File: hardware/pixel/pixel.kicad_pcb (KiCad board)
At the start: 2 copper layers, 20 x 20 mm, 13 parts, among them J1 IN (male), J2 OUT (female), U1 WS2814F

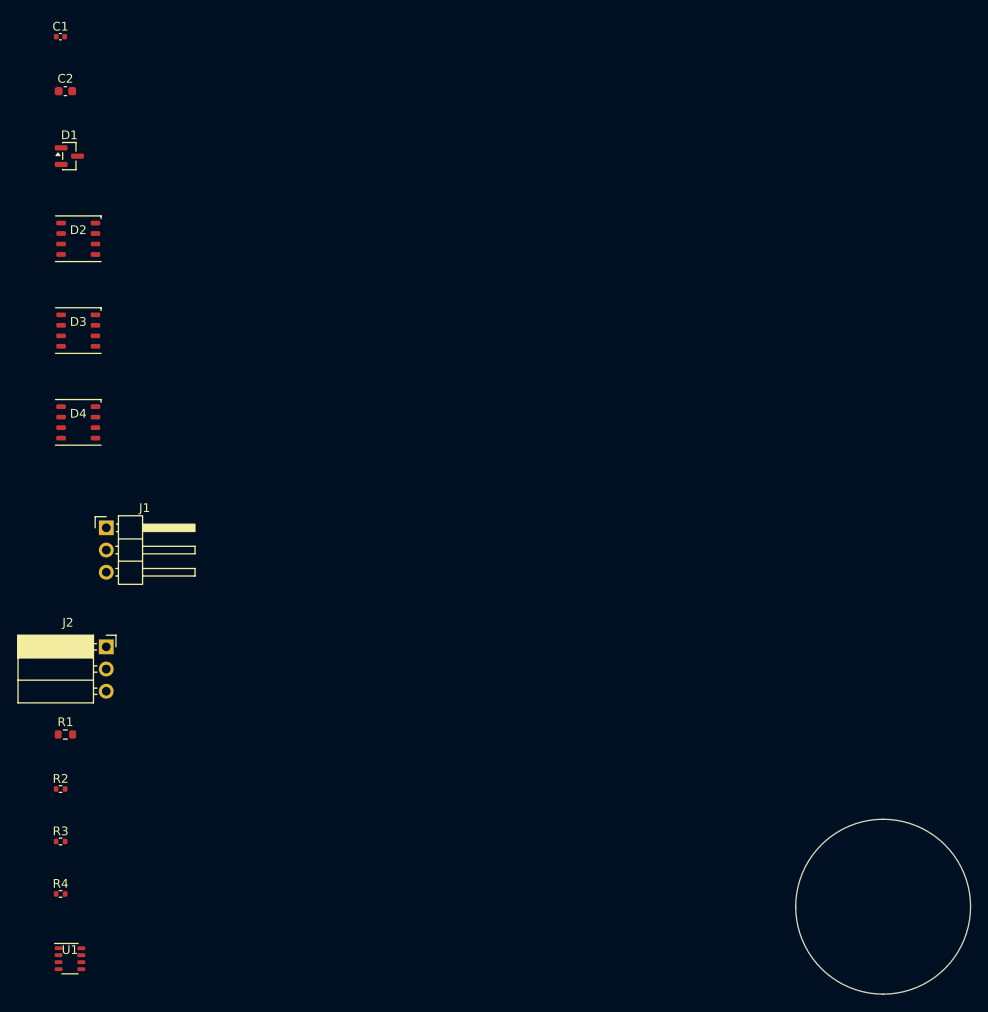
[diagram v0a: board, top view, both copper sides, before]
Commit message: Pixel PCB: provisional fit-study placement
Headers on the bottom along the south rim (estimated plug width),
LEDs in a centered triangle, U1 and passives around them. No
courtyard overlaps; only unrouted-connection DRC errors remain.
Also refreshes all footprints from their libraries (the schematic
import had left them out of sync).

Co-Authored-By: Claude Opus 5.5 <noreply@anthropic.com>
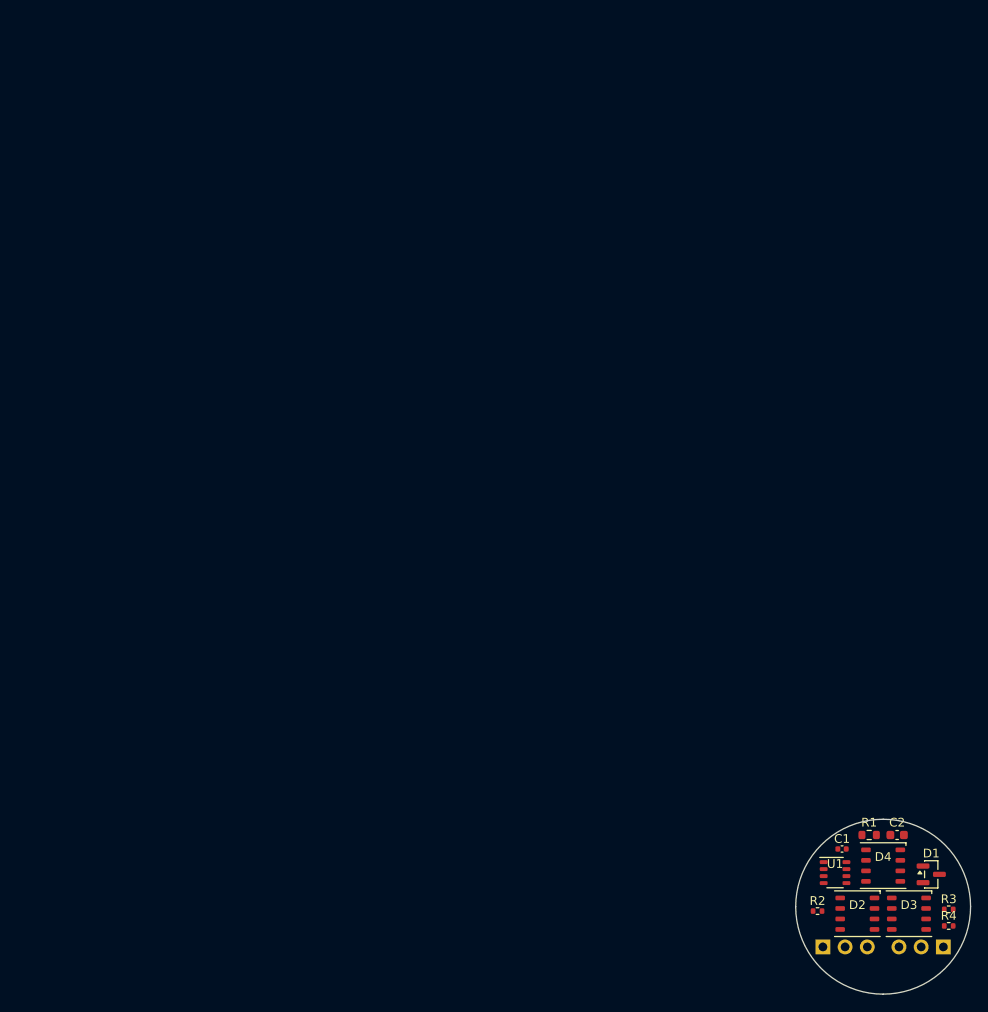
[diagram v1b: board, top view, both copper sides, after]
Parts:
- J1, J2: moved to B.Cu
- moved C1 128.9 mm to (95.3, 93.4)
- moved D1 128.3 mm to (105.5, 96.3)
- moved C2 127.6 mm to (101.6, 91.8)
- moved D2 117.9 mm to (97.0, 100.8)
- moved D3 116.1 mm to (103.0, 100.8)
- moved D4 105.1 mm to (100.0, 95.3)
- moved R3 101.9 mm to (107.5, 100.3)
- moved J2 101.7 mm to (106.9, 104.6), turned to 90 degrees
- moved R4 101.6 mm to (107.5, 102.2)
- moved J1 94.9 mm to (93.1, 104.6), turned to -90 degrees
- moved R1 92.6 mm to (98.4, 91.8)
- moved U1 88.1 mm to (94.5, 96.1)
- moved R2 87.7 mm to (92.5, 100.5)

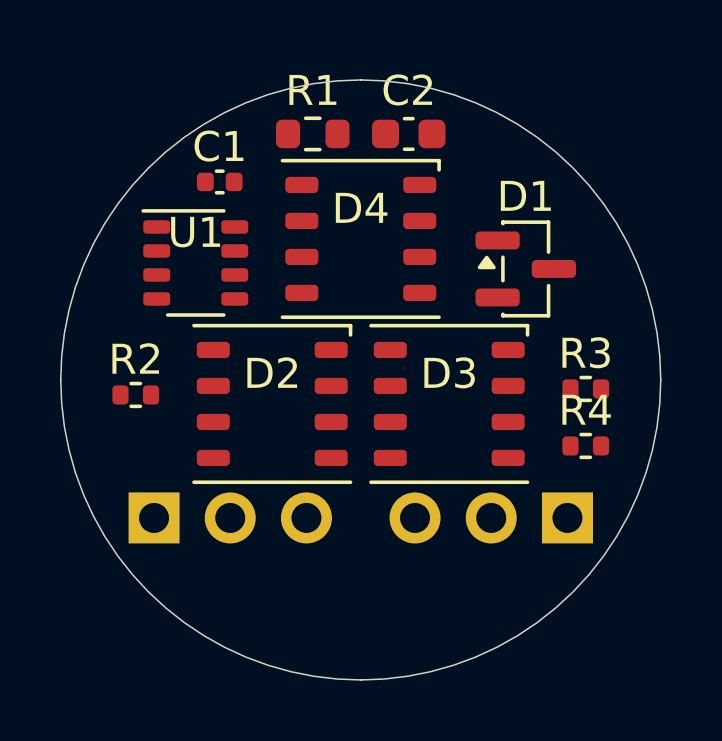
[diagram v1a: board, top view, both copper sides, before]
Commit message: Pixel PCB: headers under the board, LEDs spaced out
Adopts the hand-tuned layout: header pin rows north of center with
their bodies running under the board, since only the headers are on
the bottom. Gives the LEDs 0.5-1 mm between bodies. Passives placed
around it; C1 sits beside U1's VDD pin. Placement score 100; only
unrouted-connection DRC errors remain.

Co-Authored-By: Claude Opus 5.5 <noreply@anthropic.com>
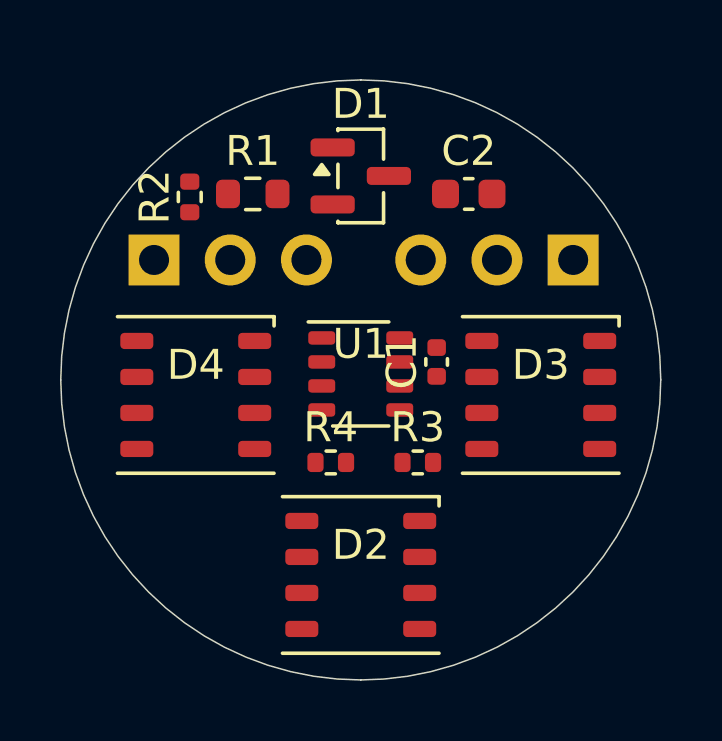
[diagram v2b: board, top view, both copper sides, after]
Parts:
- moved C1 9.40 mm to (102.5, 99.4), turned to 90 degrees
- moved J2 8.60 mm to (107.1, 96.0)
- moved J1 8.60 mm to (93.1, 96.0)
- moved R4 8.52 mm to (99.0, 102.8)
- moved D4 7.57 mm to (94.5, 100.5)
- moved R2 6.84 mm to (94.3, 93.9), turned to 90 degrees
- moved U1 6.63 mm to (100.0, 99.8)
- moved D2 6.42 mm to (100.0, 106.5)
- moved D1 6.31 mm to (100.0, 93.2)
- moved R3 6.11 mm to (101.9, 102.8)
- moved D3 3.06 mm to (106.0, 100.5)
- moved C2 2.83 mm to (103.6, 93.8)
- moved R1 2.83 mm to (96.4, 93.8)
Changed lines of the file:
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@@
 	(footprint "village:FSOP-8_1.65x3.25mm_P0.8mm"
 		(layer "F.Cu")
-		(at 94.5 96.1)
+		(at 100 99.8)
 		(descr "FSOP-8, 1.65x3.25mm body, 0.8mm pitch, 2.85mm lead span (Worldsemi WS2814F, datasheet V1.1 p.6). Land: 0.9x0.45mm pads, 0.3mm toe / 0.2mm heel. Not yet verified on a fabricated board.")
 		(property "Reference" "U1"
@@
 	(footprint "village:LED_Honglitronic_HL-5050RGBW_5.0x5.0mm_P1.2mm"
 		(layer "F.Cu")
-		(at 102.95 100.8)
+		(at 106 100.5)
 		(descr "RGBW 5050 LED, 8 pads, Honglitronic HL-5050RGBW-S1 (spec B-18-A-1651 rev A/2 p.3), recommended land pattern: 1.1x0.54mm pads, 2.83mm inner gap, 1.2mm pitch. Top view: anodes 1/3/5/7 (W/B/G/R) on the right, cathodes 2/4/6/8 on the left; the part's corner mark is at pin 2. Datasheet top and bottom views disagree on mirroring: verify on a sample before fab.")
 		(property "Reference" "D3"
@@
 	(footprint "Resistor_SMD:R_0402_1005Metric"
 		(layer "F.Cu")
-		(at 92.5 100.5)
+		(at 94.3 93.9 90)
 		(descr "Resistor SMD 0402 (1005 Metric), square (rectangular) end terminal, IPC-7351 nominal, (Body size source: IPC-SM-782 page 72, https://www.pcb-3d.com/wordpress/wp-content/uploads/ipc-sm-782a_amendment_1_and_2.pdf)")
 		(tags "resistor")
 		(property "Reference" "R2"
-			(at 0 -1.17 0)
+			(at 0 -1.17 90)
 			(unlocked yes)
 			(layer "F.SilkS")
@@
 		)
 		(property "Value" "1k"
-			(at 0 1.170001 0)
+			(at 0 1.170001 90)
 			(unlocked yes)
 			(layer "F.SilkS")
@@
 		)
 		(property "Datasheet" ""
-			(at 0 0 0)
+			(at 0 0 90)
 			(layer "F.Fab")
 			(hide yes)
@@
 		)
 		(property "Description" ""
-			(at 0 0 0)
+			(at 0 0 90)
 			(layer "F.Fab")
 			(hide yes)
@@
 		)
 		(property "KiLib_Generator" "SMD_2terminal_chip_molded"
-			(at 0 0 0)
+			(at 0 0 90)
 			(unlocked yes)
 			(layer "F.SilkS")
@@
 		)
 		(fp_text user "${REFERENCE}"
-			(at 0 0 0)
+			(at 0 0 90)
 			(unlocked yes)
 			(layer "F.Fab")
@@
 		)
 		(pad "1" smd roundrect
-			(at -0.51 0)
+			(at -0.51 0 90)
 			(size 0.54 0.64)
 			(layers "F.Cu" "F.Mask" "F.Paste")
@@
 		)
 		(pad "2" smd roundrect
-			(at 0.51 0)
+			(at 0.51 0 90)
 			(size 0.54 0.64)
 			(layers "F.Cu" "F.Mask" "F.Paste")
@@
 	(footprint "Capacitor_SMD:C_0402_1005Metric"
 		(layer "F.Cu")
-		(at 95.3 93.4)
+		(at 102.53 99.4 90)
 		(descr "Capacitor SMD 0402 (1005 Metric), square (rectangular) end terminal, IPC-7351 nominal, (Body size source: IPC-SM-782 page 76, https://www.pcb-3d.com/wordpress/wp-content/uploads/ipc-sm-782a_amendment_1_and_2.pdf)")
 		(tags "capacitor")
 		(property "Reference" "C1"
-			(at 0 -1.159999 0)
+			(at 0 -1.159999 90)
 			(unlocked yes)
 			(layer "F.SilkS")
@@
 		)
 		(property "Value" "100n"
-			(at 0 1.16 0)
+			(at 0 1.16 90)
 			(unlocked yes)
 			(layer "F.SilkS")
@@
 		)
 		(property "Datasheet" ""
-			(at 0 0 0)
+			(at 0 0 90)
 			(layer "F.Fab")
 			(hide yes)
@@
 		)
 		(property "Description" ""
-			(at 0 0 0)
+			(at 0 0 90)
 			(layer "F.Fab")
 			(hide yes)
@@
 		)
 		(property "KiLib_Generator" "SMD_2terminal_chip_molded"
-			(at 0 0 0)
+			(at 0 0 90)
 			(unlocked yes)
 			(layer "F.SilkS")
@@
 		)
 		(fp_text user "${REFERENCE}"
-			(at 0 0 0)
+			(at 0 0 90)
 			(unlocked yes)
 			(layer "F.Fab")
@@
 		)
 		(pad "1" smd roundrect
-			(at -0.48 0)
+			(at -0.48 0 90)
 			(size 0.56 0.62)
 			(layers "F.Cu" "F.Mask" "F.Paste")
@@
 		)
 		(pad "2" smd roundrect
-			(at 0.48 0)
+			(at 0.48 0 90)
 			(size 0.56 0.62)
 			(layers "F.Cu" "F.Mask" "F.Paste")
@@
 	(footprint "Capacitor_SMD:C_0603_1608Metric"
 		(layer "F.Cu")
-		(at 101.6 91.8)
+		(at 103.6 93.8)
 		(descr "Capacitor SMD 0603 (1608 Metric), square (rectangular) end terminal, IPC-7351 nominal, (Body size source: IPC-SM-782 page 76, https://www.pcb-3d.com/wordpress/wp-content/uploads/ipc-sm-782a_amendment_1_and_2.pdf)")
 		(tags "capacitor")
@@
 	(footprint "village:LED_Honglitronic_HL-5050RGBW_5.0x5.0mm_P1.2mm"
 		(layer "F.Cu")
-		(at 100 95.3)
+		(at 94.5 100.5)
 		(descr "RGBW 5050 LED, 8 pads, Honglitronic HL-5050RGBW-S1 (spec B-18-A-1651 rev A/2 p.3), recommended land pattern: 1.1x0.54mm pads, 2.83mm inner gap, 1.2mm pitch. Top view: anodes 1/3/5/7 (W/B/G/R) on the right, cathodes 2/4/6/8 on the left; the part's corner mark is at pin 2. Datasheet top and bottom views disagree on mirroring: verify on a sample before fab.")
 		(property "Reference" "D4"
@@
 	(footprint "Resistor_SMD:R_0603_1608Metric"
 		(layer "F.Cu")
-		(at 98.4 91.8)
+		(at 96.4 93.8)
 		(descr "Resistor SMD 0603 (1608 Metric), square (rectangular) end terminal, IPC-7351 nominal, (Body size source: IPC-SM-782 page 72, https://www.pcb-3d.com/wordpress/wp-content/uploads/ipc-sm-782a_amendment_1_and_2.pdf)")
 		(tags "resistor")
@@
 	(footprint "village:LED_Honglitronic_HL-5050RGBW_5.0x5.0mm_P1.2mm"
 		(layer "F.Cu")
-		(at 97.05 100.8)
+		(at 100 106.5)
 		(descr "RGBW 5050 LED, 8 pads, Honglitronic HL-5050RGBW-S1 (spec B-18-A-1651 rev A/2 p.3), recommended land pattern: 1.1x0.54mm pads, 2.83mm inner gap, 1.2mm pitch. Top view: anodes 1/3/5/7 (W/B/G/R) on the right, cathodes 2/4/6/8 on the left; the part's corner mark is at pin 2. Datasheet top and bottom views disagree on mirroring: verify on a sample before fab.")
 		(property "Reference" "D2"
@@
 	(footprint "Resistor_SMD:R_0402_1005Metric"
 		(layer "F.Cu")
-		(at 107.5 100.3)
+		(at 101.9 102.75)
 		(descr "Resistor SMD 0402 (1005 Metric), square (rectangular) end terminal, IPC-7351 nominal, (Body size source: IPC-SM-782 page 72, https://www.pcb-3d.com/wordpress/wp-content/uploads/ipc-sm-782a_amendment_1_and_2.pdf)")
 		(tags "resistor")
@@
 	(footprint "Package_TO_SOT_SMD:SOT-23"
 		(layer "F.Cu")
-		(at 105.5 96.3)
+		(at 100 93.2)
 		(descr "SOT, 3 Pin (JEDEC TO-236 Var AB https://www.jedec.org/document_search?search_api_views_fulltext=TO-236)")
 		(tags "SOT TO_SOT_SMD")
@@
 	(footprint "Resistor_SMD:R_0402_1005Metric"
 		(layer "F.Cu")
-		(at 107.5 102.2)
+		(at 99 102.75)
 		(descr "Resistor SMD 0402 (1005 Metric), square (rectangular) end terminal, IPC-7351 nominal, (Body size source: IPC-SM-782 page 72, https://www.pcb-3d.com/wordpress/wp-content/uploads/ipc-sm-782a_amendment_1_and_2.pdf)")
 		(tags "resistor")
@@
 	(footprint "Connector_PinSocket_2.54mm:PinSocket_1x03_P2.54mm_Horizontal"
 		(layer "B.Cu")
-		(at 106.89 104.6 90)
+		(at 107.08 96 90)
 		(descr "Through hole angled socket strip, 1x03, 2.54mm pitch, 8.51mm socket length, single row (from Kicad 4.0.7), script generated")
 		(tags "Through hole angled socket strip THT 1x03 2.54mm single row")
@@
 	(footprint "Connector_PinHeader_2.54mm:PinHeader_1x03_P2.54mm_Horizontal"
 		(layer "B.Cu")
-		(at 93.11 104.6 -90)
+		(at 93.110001 96 -90)
 		(descr "Through hole angled pin header, 1x03, 2.54mm pitch, 6mm pin length, single row")
 		(tags "Through hole angled pin header THT 1x03 2.54mm single row")
